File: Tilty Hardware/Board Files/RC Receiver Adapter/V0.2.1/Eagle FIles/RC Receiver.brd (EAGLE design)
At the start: 38.1 x 50.8 mm, 29 parts, among them U1 ATMEGA328P, U2 LM2931, U3 AP7313SOT23R, U4 C74HC407514-SOIC, Y1 16MHz

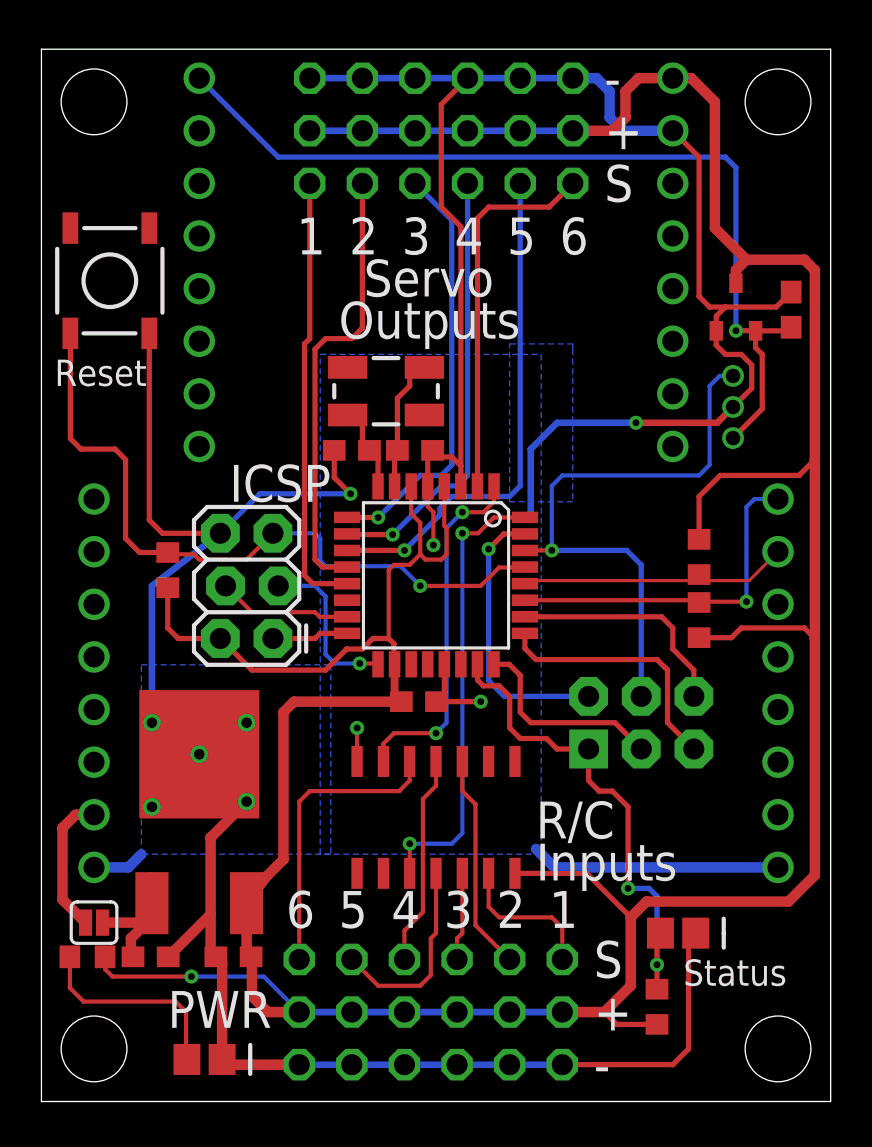
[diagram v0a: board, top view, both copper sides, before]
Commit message: Semi-major revision to R/C Receiver adapter
All signals are now read by individual inputs and are no longer
interrupt driven. However the connection order will no longer matter,
and servo and R/C channels can be mixed.
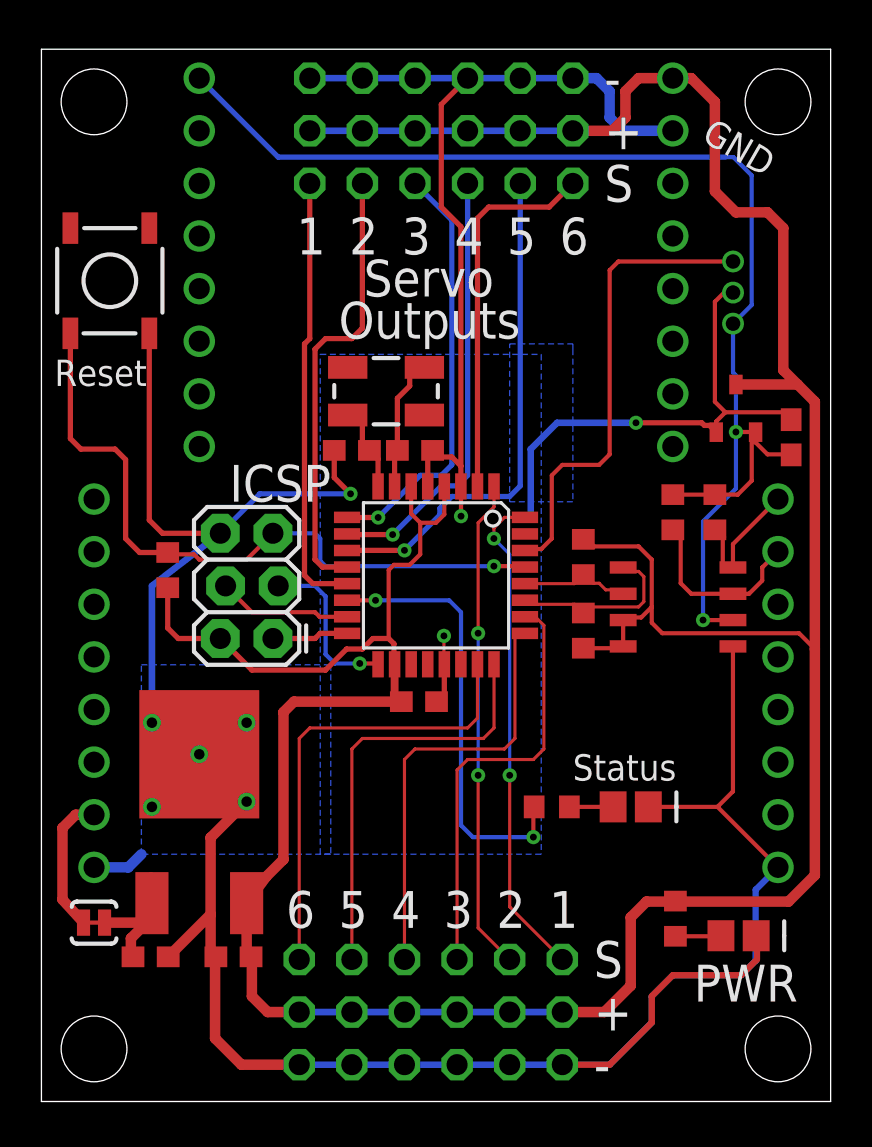
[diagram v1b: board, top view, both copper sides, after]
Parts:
- removed JP10: (no value), SparkFun-Connectors:2X3-NS
- removed U4: C74HC407514-SOIC, My Parts:14-SOIC
- added R6, R7: (no value), resistor:R0603
- added U$1: PCA9306, My Parts:SOIC-8
- SJ1: value SOLDERJUMPERNC -> SOLDERJUMPERTRACE; device SparkFun-Passives:SJ_2S -> SparkFun-Passives:SJ_2S-TRACE
- moved R5 28.4 mm to (30.6, 8.83), turned to 90 degrees
- moved D2 26.5 mm to (33.7, 8.00)
- moved R4 10.9 mm to (24.6, 14.2), turned to 180 degrees
- moved D1 6.51 mm to (28.4, 14.2)
- moved C4 6.16 mm to (36.2, 32.1)
- moved R2 5.61 mm to (26.2, 22.7)
- moved R3 5.59 mm to (26.2, 26.3)
- moved JP8 5.52 mm to (35.0, 39.1)
- moved U3 4.89 mm to (33.5, 33.5)
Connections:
- removed net A1: JP10.3, U1.24
- removed net A2: JP10.5, U1.25
- removed net A3: JP10.6, U1.26
- removed net EVEN_CHAN: U1.1, U4.P$6
- removed net ODD_CHAN: U1.32, U4.P$10
- removed net SCL: JP3.7, R3.1, U1.28
- removed net SDA: JP3.8, R2.1, U1.27
- removed net SIGNAL_1: JP7.1, U4.P$13
- removed net SIGNAL_2: JP7.4, U4.P$3
- removed net SIGNAL_3: JP7.7, U4.P$12
- removed net SIGNAL_4: JP7.10, U4.P$4
- removed net SIGNAL_5: JP7.13, U4.P$11
- removed net SIGNAL_6: JP7.16, U4.P$5
- new net 3V_SCL: JP3.7, R6.1, U$1.P$3
- new net 3V_SDA: JP3.8, R7.1, U$1.P$4
- new net 5V_SCL: R3.1, U$1.P$6, U1.28
- new net 5V_SDA: R2.1, U$1.P$5, U1.27
- new net N$6: D1.1, R4.1
- new net RC_IN1: JP7.1, U1.32
- new net RC_IN2: JP7.4, U1.1
- new net RC_IN3: JP7.7, U1.26
- new net RC_IN4: JP7.10, U1.25
- new net RC_IN5: JP7.13, U1.24
- new net RC_IN6: JP7.16, U1.23
- net +3V3: now also R6.2, R7.2, U$1.P$2
- net +5V: now also U$1.P$7, U$1.P$8; no longer R4.2, U4.P$14
- net ARDUINO_TX: no longer JP10.2
- net GND: now also U$1.P$1; no longer U4.P$7
- net SATELLITE_TX: no longer JP10.4
- net STATUS_LED: now also R4.2, U1.14; no longer D1.1, JP10.1, R4.1, U1.23
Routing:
- net RC_IN1: track 0.00 -> 23.9 mm, vias 0 -> 2
- net RC_IN2: track 0.00 -> 23.8 mm, vias 0 -> 2
- net RC_IN6: track 0.00 -> 22.3 mm
- net ODD_CHAN: track 22.0 -> 0.00 mm, vias 2 -> 0
- net RC_IN4: track 0.00 -> 20.9 mm
- net RC_IN3: track 0.00 -> 20.8 mm
- net RC_IN5: track 0.00 -> 20.5 mm
- net +3V3: track 44.2 -> 62.4 mm, vias 1 -> 2
- net EVEN_CHAN: track 17.3 -> 0.00 mm, vias 2 -> 0
- net SDA: track 17.0 -> 0.00 mm, vias 1 -> 0
- net SIGNAL_6: track 14.3 -> 0.00 mm
- net +5V: track 182.2 -> 168.5 mm, vias 1 -> 0
- net ARDUINO_TX: track 13.5 -> 0.00 mm, vias 1 -> 0
- net SCL: track 13.3 -> 0.00 mm
- net A2: track 12.4 -> 0.00 mm
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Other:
- board text removed: "A0"
- board text removed: "A1"
- board text removed: "A2"
- board text removed: "A3"
- board text removed: "Extra"
- board text removed: "Inputs"
- board text removed: "Pins"
- board text removed: "R/C"
- board text removed: "RX"
- board text removed: "TX"

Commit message: Updated R/C adapter silkscreen
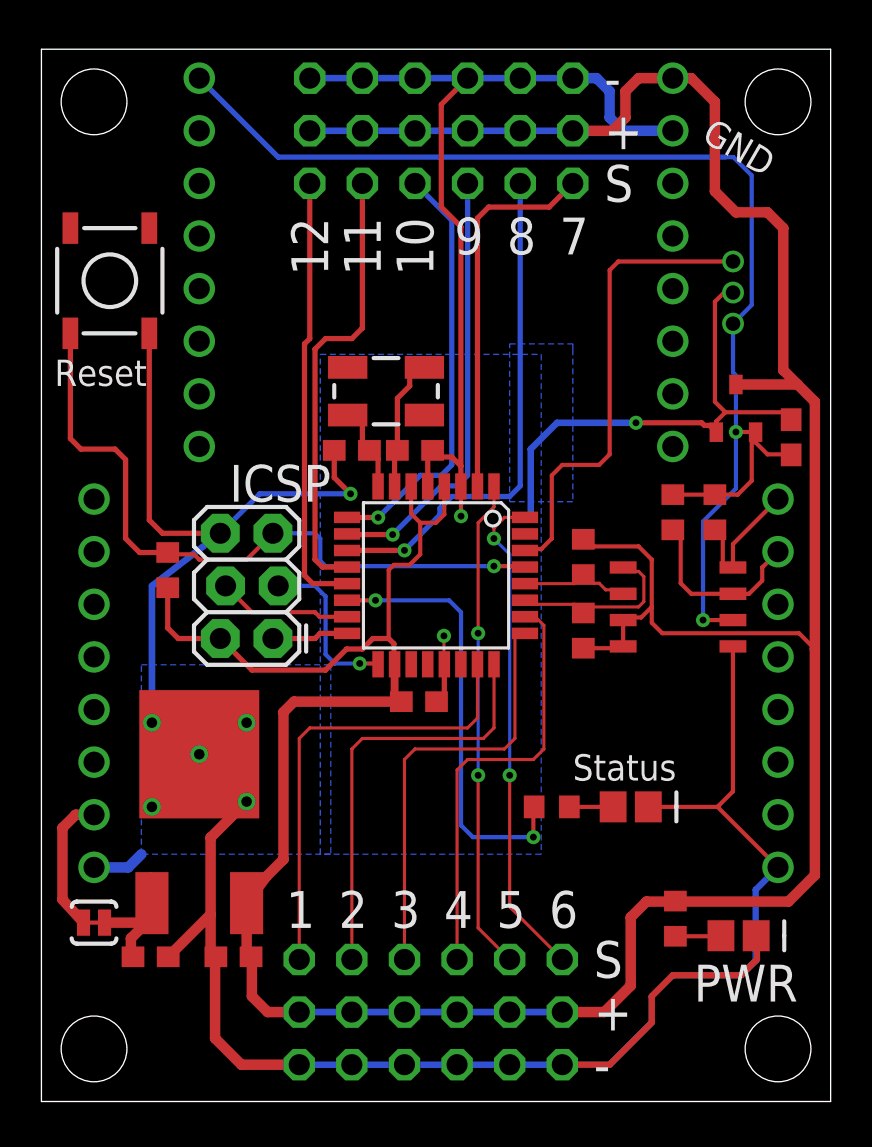
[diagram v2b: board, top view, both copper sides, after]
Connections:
- net ARDUINO_TX renamed TX
- net SATELLITE_TX renamed RX
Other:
- board text added: "10"
- board text added: "11"
- board text added: "12"
- board text added: "7"
- board text added: "8"
- board text added: "9"
- board text removed: "Outputs"
- board text removed: "Servo"
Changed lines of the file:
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@@
 <text x="26.67" y="3.429" size="1.778" layer="25" ratio="12">+</text>
 <text x="26.67" y="0.889" size="1.778" layer="25" ratio="12">-</text>
-<text x="24.511" y="8.382" size="1.778" layer="25" ratio="12">1</text>
-<text x="21.971" y="8.382" size="1.778" layer="25" ratio="12">2</text>
-<text x="19.431" y="8.382" size="1.778" layer="25" ratio="12">3</text>
-<text x="16.891" y="8.382" size="1.778" layer="25" ratio="12">4</text>
-<text x="14.351" y="8.382" size="1.778" layer="25" ratio="12">5</text>
-<text x="11.811" y="8.382" size="1.778" layer="25" ratio="12">6</text>
+<text x="24.511" y="8.382" size="1.778" layer="25" ratio="12">6</text>
+<text x="21.971" y="8.382" size="1.778" layer="25" ratio="12">5</text>
+<text x="19.431" y="8.382" size="1.778" layer="25" ratio="12">4</text>
+<text x="16.891" y="8.382" size="1.778" layer="25" ratio="12">3</text>
+<text x="14.351" y="8.382" size="1.778" layer="25" ratio="12">2</text>
+<text x="11.811" y="8.382" size="1.778" layer="25" ratio="12">1</text>
 <hole x="2.54" y="2.54" drill="3.175"/>
 <hole x="2.54" y="48.26" drill="3.175"/>
 <hole x="35.56" y="48.26" drill="3.175"/>
 <hole x="35.56" y="2.54" drill="3.175"/>
-<text x="25.019" y="40.894" size="1.778" layer="25" ratio="12">6</text>
-<text x="22.479" y="40.894" size="1.778" layer="25" ratio="12">5</text>
-<text x="19.939" y="40.894" size="1.778" layer="25" ratio="12">4</text>
-<text x="17.399" y="40.894" size="1.778" layer="25" ratio="12">3</text>
-<text x="14.859" y="40.894" size="1.778" layer="25" ratio="12">2</text>
-<text x="12.319" y="40.894" size="1.778" layer="25" ratio="12">1</text>
-<text x="15.5575" y="38.862" size="1.778" layer="25" ratio="12">Servo</text>
-<text x="14.351" y="36.83" size="1.778" layer="25" ratio="12">Outputs</text>
+<text x="25.019" y="40.894" size="1.778" layer="25" ratio="12">7</text>
+<text x="22.479" y="40.894" size="1.778" layer="25" ratio="12">8</text>
+<text x="19.939" y="40.894" size="1.778" layer="25" ratio="12">9</text>
+<text x="18.923" y="39.878" size="1.778" layer="25" ratio="12" rot="R90">10</text>
+<text x="16.383" y="39.878" size="1.778" layer="25" ratio="12" rot="R90">11</text>
+<text x="13.843" y="39.878" size="1.778" layer="25" ratio="12" rot="R90">12</text>
 <text x="27.178" y="48.514" size="1.778" layer="25" ratio="12">-</text>
 <text x="27.178" y="45.974" size="1.778" layer="25" ratio="12">+</text>
@@
 <wire x1="21.082" y1="8.382" x2="22.606" y2="6.858" width="0.1524" layer="1"/>
 </signal>
-<signal name="SATELLITE_TX">
+<signal name="RX">
 <contactref element="JP8" pad="P$3"/>
 <contactref element="U1" pad="30"/>
@@
 </polygon>
 </signal>
-<signal name="ARDUINO_TX">
+<signal name="TX">
 <contactref element="U1" pad="31"/>
 </signal>
